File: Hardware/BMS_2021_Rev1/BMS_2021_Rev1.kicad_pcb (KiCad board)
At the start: 2 copper layers, 210.8 x 76.2 mm, 117 parts, among them Q1 2N7002PW, Q2 IRFS7530TRL7PP, Q3 IRFS7530TRL7PP, Q4 2N7002, Q5 2N7002PW, SW1 Relay_SPST, U1 TM4C129E_Launchpad, U2 ACS759ECB-200B-PFF-T, U3 TL3474ACPWR, U4 TL3474ACPWR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

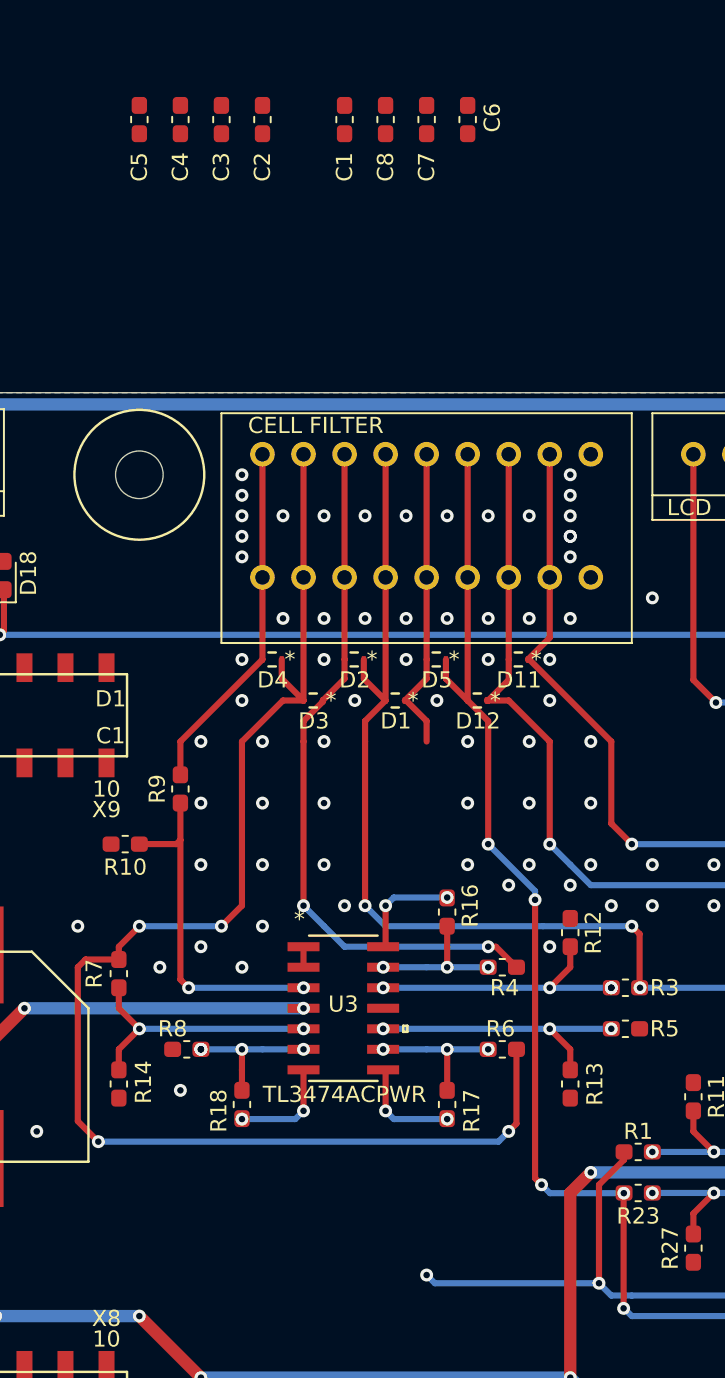
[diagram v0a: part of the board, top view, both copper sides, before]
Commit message: had forgot to add in cellFIlter Caps, added it (and kept the circuit well-grounded)
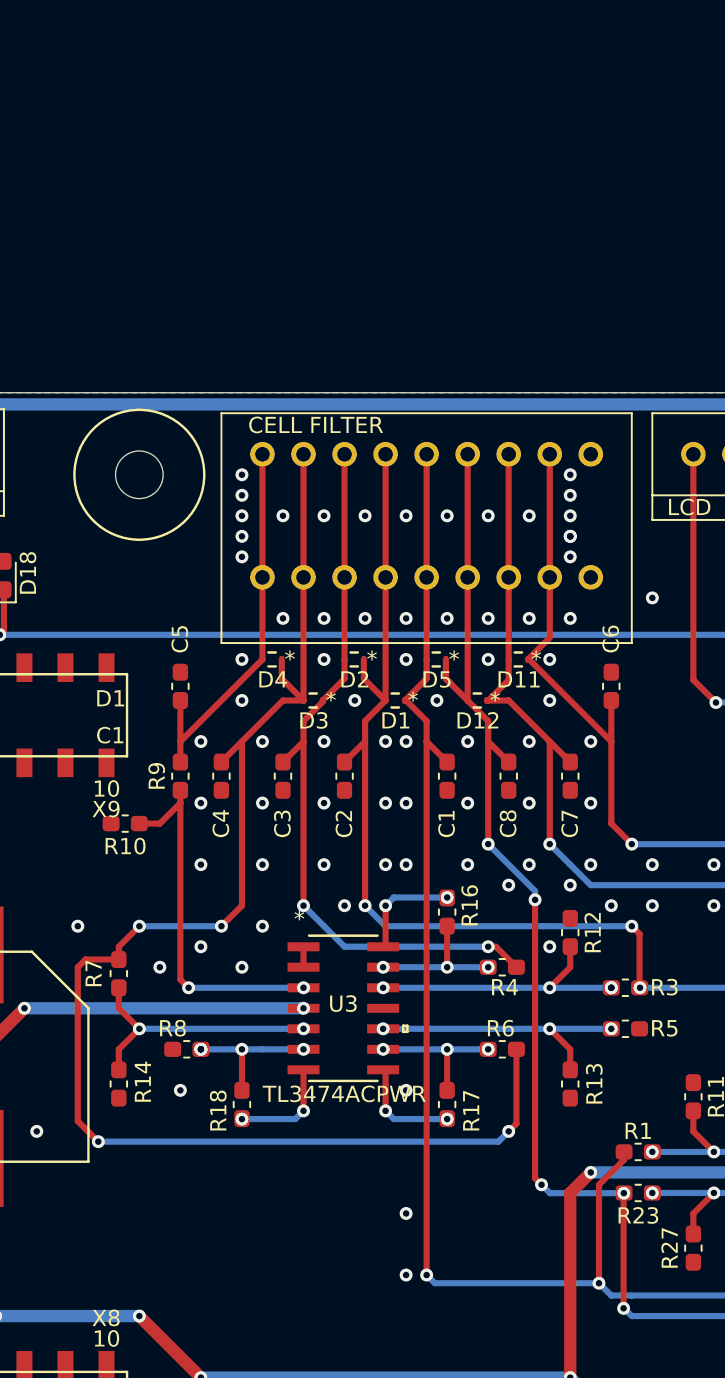
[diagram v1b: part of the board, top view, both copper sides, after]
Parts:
- moved C7 41.6 mm to (114.3, 49.1)
- moved C8 41.3 mm to (110.5, 49.1)
- moved C1 41.1 mm to (106.7, 49.1)
- moved C2 41.0 mm to (100.3, 49.1)
- moved C3 40.8 mm to (96.5, 49.1)
- moved C4 40.7 mm to (92.7, 49.1)
- moved C6 36.2 mm to (116.8, 43.6), turned to 270 degrees
- moved C5 35.2 mm to (90.2, 43.6), turned to 270 degrees
- moved R10 1.27 mm to (86.8, 52.1)
- moved R9 0.79 mm to (90.2, 49.1)
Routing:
- net cell_5_extension: track 52.7 -> 87.5 mm
- net /cell_8: track 88.7 -> 91.2 mm
- net /cell_6: track 97.9 -> 100.0 mm
- net /cell_4: track 67.7 -> 69.5 mm
- net /cell_3: track 43.8 -> 45.5 mm
- net /cell_2: track 87.8 -> 89.6 mm
- net /cell_7: track 98.9 -> 100.7 mm
- net /cell_1: track 21.9 -> 23.7 mm
- net Net-(R10-Pad1): track 21.4 -> 22.6 mm
- net GND: vias 131 -> 140

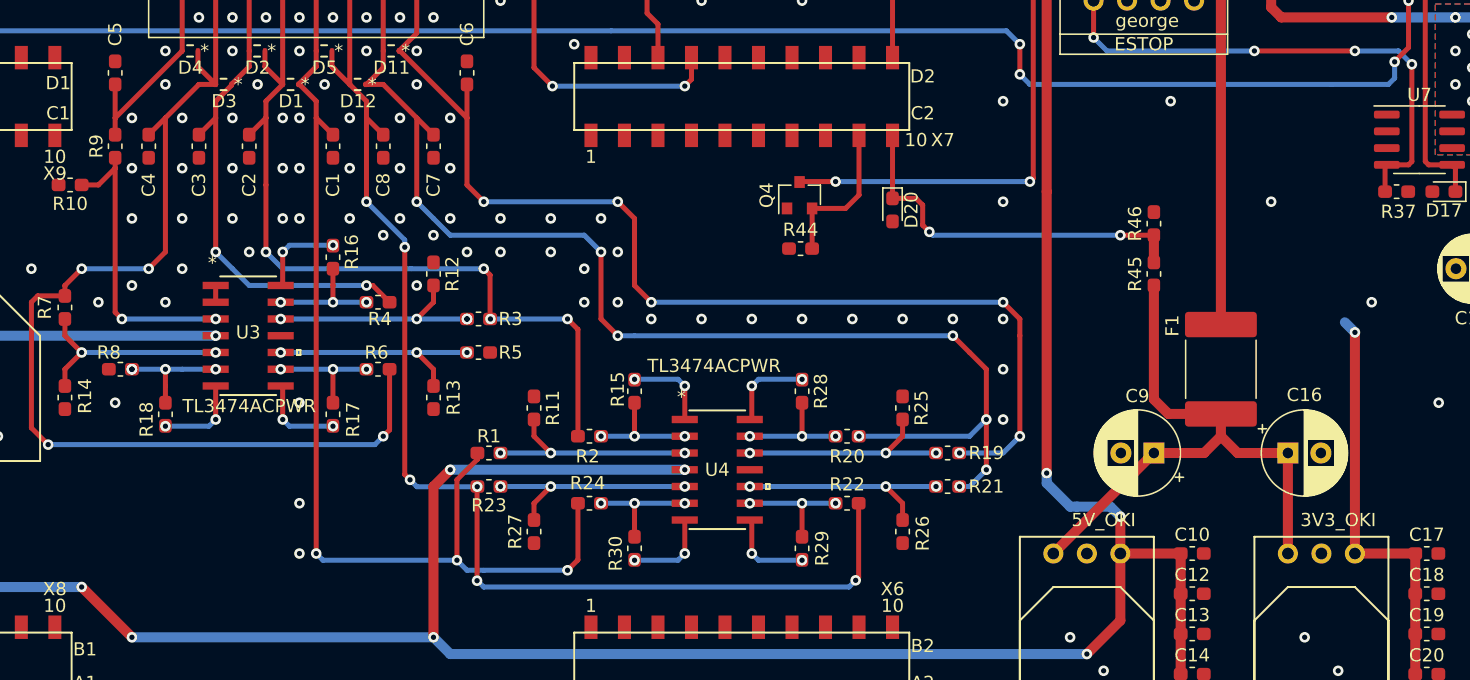
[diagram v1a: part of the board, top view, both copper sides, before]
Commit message: more gnd planing done btwn cell lines
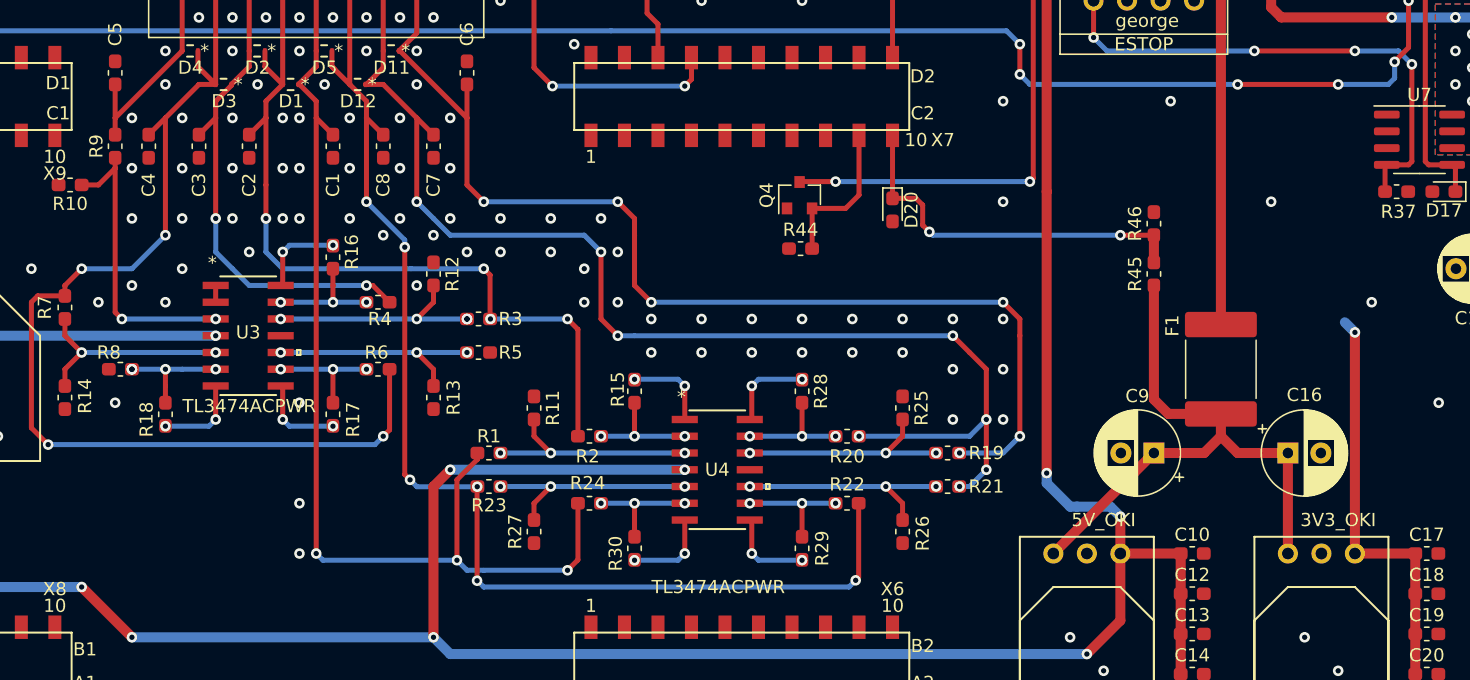
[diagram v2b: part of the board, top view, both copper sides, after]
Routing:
- net /cell_2: track 89.6 -> 88.9 mm
- net /V_out_sense: vias 6 -> 8
- net GND: vias 140 -> 148
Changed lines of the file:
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@@
     (thickness 1.6)
     (drawings 97)
-    (tracks 1187)
+    (tracks 1199)
     (zones 0)
     (modules 117)
@@
       (effects (font (size 1 1) (thickness 0.15)))
     )
-    (fp_text value TL3474ACPWR (at -0.2413 -7.874) (layer F.SilkS)
+    (fp_text value TL3474ACPWR (at 0.0762 8.89) (layer F.SilkS)
       (effects (font (size 1 1) (thickness 0.15)))
     )
@@
   (via (at 104.14 50.8) (size 0.8) (drill 0.4) (layers F.Cu B.Cu) (net 3))
   (via (at 102.87 54.61) (size 0.8) (drill 0.4) (layers F.Cu B.Cu) (net 3))
+  (via (at 130.81 64.77) (size 0.8) (drill 0.4) (layers F.Cu B.Cu) (net 3))
+  (via (at 134.62 64.77) (size 0.8) (drill 0.4) (layers F.Cu B.Cu) (net 3))
+  (via (at 138.43 64.77) (size 0.8) (drill 0.4) (layers F.Cu B.Cu) (net 3))
+  (via (at 142.24 64.77) (size 0.8) (drill 0.4) (layers F.Cu B.Cu) (net 3))
+  (via (at 146.05 64.77) (size 0.8) (drill 0.4) (layers F.Cu B.Cu) (net 3))
+  (via (at 149.86 64.77) (size 0.8) (drill 0.4) (layers F.Cu B.Cu) (net 3))
+  (via (at 153.67 66.04) (size 0.8) (drill 0.4) (layers F.Cu B.Cu) (net 3))
+  (via (at 153.67 69.85) (size 0.8) (drill 0.4) (layers F.Cu B.Cu) (net 3))
   (segment (start 102.87 29.21) (end 102.87 36.83) (width 0.381) (layer F.Cu) (net 4))
   (segment (start 102.87 36.83) (end 102.87 44.45) (width 0.381) (layer F.Cu) (net 4))
@@
   (segment (start 118.59 58.9) (end 118.11 58.42) (width 0.381) (layer F.Cu) (net 4))
   (segment (start 118.11 58.42) (end 112.6015 58.42) (width 0.381) (layer B.Cu) (net 4))
-  (via (at 101.6 57.15) (size 0.8) (drill 0.4) (layers F.Cu B.Cu) (net 4))
   (segment (start 112.6015 58.42) (end 102.87 58.42) (width 0.381) (layer B.Cu) (net 4))
   (segment (start 102.87 58.42) (end 101.6 57.15) (width 0.381) (layer B.Cu) (net 4))
-  (segment (start 101.6 57.15) (end 101.6 52.07) (width 0.381) (layer F.Cu) (net 4))
   (segment (start 101.6 52.07) (end 101.6 46.99) (width 0.381) (layer F.Cu) (net 4))
   (segment (start 100.33 48.26) (end 101.6 46.99) (width 0.381) (layer F.Cu) (net 4))
+  (via (at 101.6 54.61) (size 0.8) (drill 0.4) (layers F.Cu B.Cu) (net 4))
+  (segment (start 101.6 57.15) (end 101.6 54.61) (width 0.381) (layer B.Cu) (net 4))
+  (segment (start 101.6 54.61) (end 101.6 52.07) (width 0.381) (layer F.Cu) (net 4))
   (segment (start 100.33 29.21) (end 100.33 36.83) (width 0.381) (layer F.Cu) (net 5))
   (segment (start 100.33 36.83) (end 100.33 41.91) (width 0.381) (layer F.Cu) (net 5))
@@
   (segment (start 98.9838 44.5262) (end 97.79 45.72) (width 0.381) (layer F.Cu) (net 5))
   (segment (start 98.9838 44.45) (end 98.9838 44.5262) (width 0.381) (layer F.Cu) (net 5))
-  (segment (start 97.79 46.99) (end 97.79 57.15) (width 0.381) (layer F.Cu) (net 5))
-  (segment (start 97.79 57.15) (end 97.79 57.15) (width 0.381) (layer F.Cu) (net 5))
-  (via (at 97.79 57.15) (size 0.8) (drill 0.4) (layers F.Cu B.Cu) (net 5))
   (segment (start 99.06 58.42) (end 97.79 57.15) (width 0.381) (layer B.Cu) (net 5))
   (via (at 109.22 59.69) (size 0.8) (drill 0.4) (layers F.Cu B.Cu) (net 5))
@@
   (segment (start 109.22 59.69) (end 100.33 59.69) (width 0.381) (layer B.Cu) (net 5))
   (segment (start 96.52 48.26) (end 97.79 46.99) (width 0.381) (layer F.Cu) (net 5))
+  (via (at 97.79 54.61) (size 0.8) (drill 0.4) (layers F.Cu B.Cu) (net 5))
+  (segment (start 97.79 57.15) (end 97.79 54.61) (width 0.381) (layer B.Cu) (net 5))
+  (segment (start 97.79 54.61) (end 97.79 46.99) (width 0.381) (layer F.Cu) (net 5))
   (segment (start 97.79 29.21) (end 97.79 36.83) (width 0.381) (layer F.Cu) (net 6))
   (segment (start 97.79 36.83) (end 97.79 44.45) (width 0.381) (layer F.Cu) (net 6))
@@
   (segment (start 97.79 44.45) (end 96.52 44.45) (width 0.381) (layer F.Cu) (net 6))
   (segment (start 96.52 44.45) (end 93.98 46.99) (width 0.381) (layer F.Cu) (net 6))
-  (segment (start 93.98 46.99) (end 93.98 57.15) (width 0.381) (layer F.Cu) (net 6))
-  (via (at 92.71 58.42) (size 0.8) (drill 0.4) (layers F.Cu B.Cu) (net 6))
-  (segment (start 93.98 57.15) (end 92.71 58.42) (width 0.381) (layer F.Cu) (net 6))
-  (segment (start 92.71 58.42) (end 87.63 58.42) (width 0.381) (layer B.Cu) (net 6))
-  (via (at 87.63 58.42) (size 0.8) (drill 0.4) (layers F.Cu B.Cu) (net 6))
-  (segment (start 86.36 60.48) (end 86.36 59.69) (width 0.381) (layer F.Cu) (net 6))
-  (segment (start 86.36 59.69) (end 87.63 58.42) (width 0.381) (layer F.Cu) (net 6))
   (via (at 110.49 71.12) (size 0.8) (drill 0.4) (layers F.Cu B.Cu) (net 6))
   (segment (start 110.97 70.64) (end 110.97 66.04) (width 0.381) (layer F.Cu) (net 6))
@@
   (segment (start 85.09 71.755) (end 109.855 71.755) (width 0.381) (layer B.Cu) (net 6))
   (segment (start 92.71 48.26) (end 93.98 46.99) (width 0.381) (layer F.Cu) (net 6))
+  (via (at 93.98 55.88) (size 0.8) (drill 0.4) (layers F.Cu B.Cu) (net 6))
+  (segment (start 93.98 46.99) (end 93.98 55.88) (width 0.381) (layer F.Cu) (net 6))
+  (segment (start 93.98 55.88) (end 91.44 58.42) (width 0.381) (layer B.Cu) (net 6))
+  (segment (start 86.36 59.69) (end 87.63 58.42) (width 0.381) (layer F.Cu) (net 6))
+  (segment (start 86.36 60.48) (end 86.36 59.69) (width 0.381) (layer F.Cu) (net 6))
+  (via (at 87.63 58.42) (size 0.8) (drill 0.4) (layers F.Cu B.Cu) (net 6))
+  (segment (start 87.63 58.42) (end 91.44 58.42) (width 0.381) (layer B.Cu) (net 6))
   (segment (start 95.25 29.21) (end 95.25 36.83) (width 0.381) (layer F.Cu) (net 7))
   (segment (start 95.25 36.83) (end 95.25 41.91) (width 0.381) (layer F.Cu) (net 7))
@@
   (segment (start 79.248 37.592) (end 79.248 40.132) (width 0.381) (layer F.Cu) (net 28))
   (segment (start 158.75 41.402) (end 158.75 43.688) (width 0.381) (layer F.Cu) (net 28))
-  (segment (start 159.512 44.45) (end 182.372 44.45) (width 0.381) (layer B.Cu) (net 28))
   (segment (start 157.734 40.386) (end 158.75 41.402) (width 0.381) (layer B.Cu) (net 28))
   (segment (start 158.75 43.688) (end 159.512 44.45) (width 0.381) (layer B.Cu) (net 28))
@@
   (segment (start 187.161282 43.978718) (end 186.69 44.45) (width 0.381) (layer B.Cu) (net 28))
   (segment (start 187.161282 42.737218) (end 187.161282 43.978718) (width 0.381) (layer B.Cu) (net 28))
-  (segment (start 182.372 44.45) (end 186.69 44.45) (width 0.381) (layer B.Cu) (net 28))
+  (via (at 175.26 44.45) (size 0.8) (drill 0.4) (layers F.Cu B.Cu) (net 28))
+  (segment (start 159.512 44.45) (end 175.26 44.45) (width 0.381) (layer B.Cu) (net 28))
+  (via (at 182.88 44.45) (size 0.8) (drill 0.4) (layers F.Cu B.Cu) (net 28))
+  (segment (start 175.26 44.45) (end 182.88 44.45) (width 0.381) (layer F.Cu) (net 28))
+  (segment (start 182.88 44.45) (end 186.69 44.45) (width 0.381) (layer B.Cu) (net 28))
   (segment (start 149.098 48.1584) (end 149.098 53.086) (width 0.381) (layer F.Cu) (net 29))
   (segment (start 168.91 57.94) (end 168.91 55.88) (width 0.762) (layer F.Cu) (net 29))

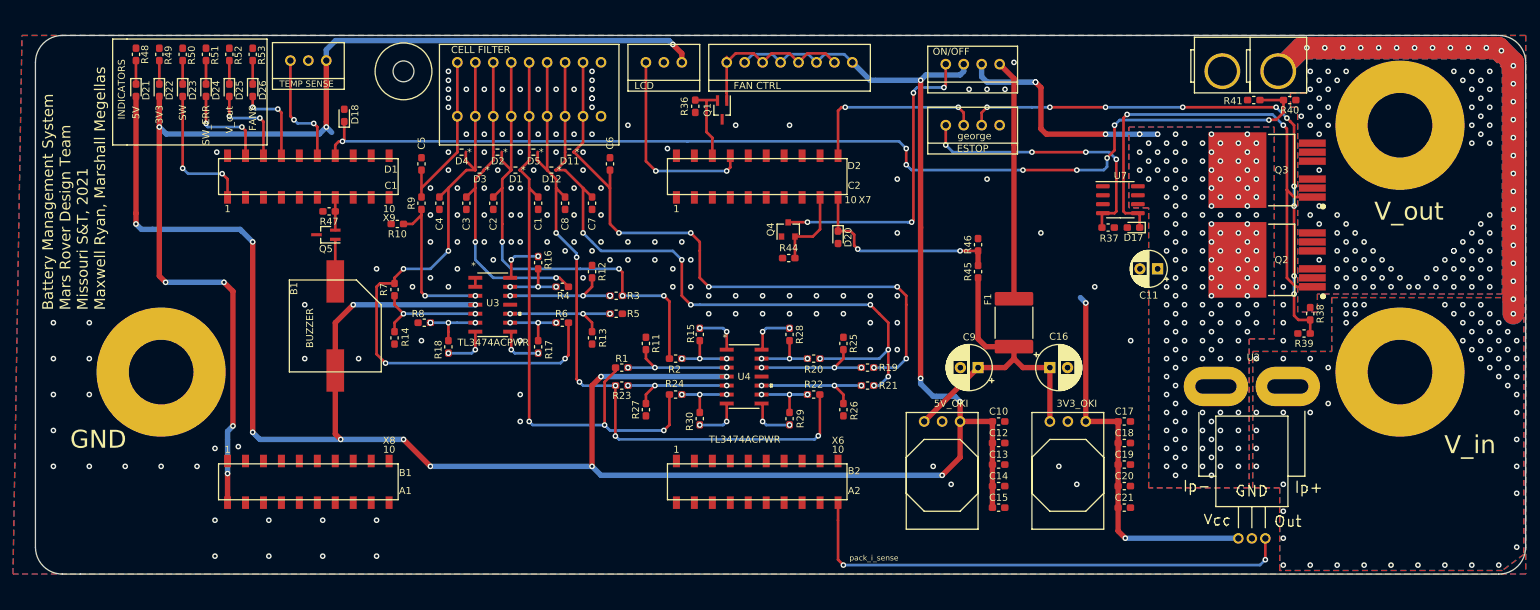
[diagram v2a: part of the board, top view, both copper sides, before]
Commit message: reinforce gnding around charging port
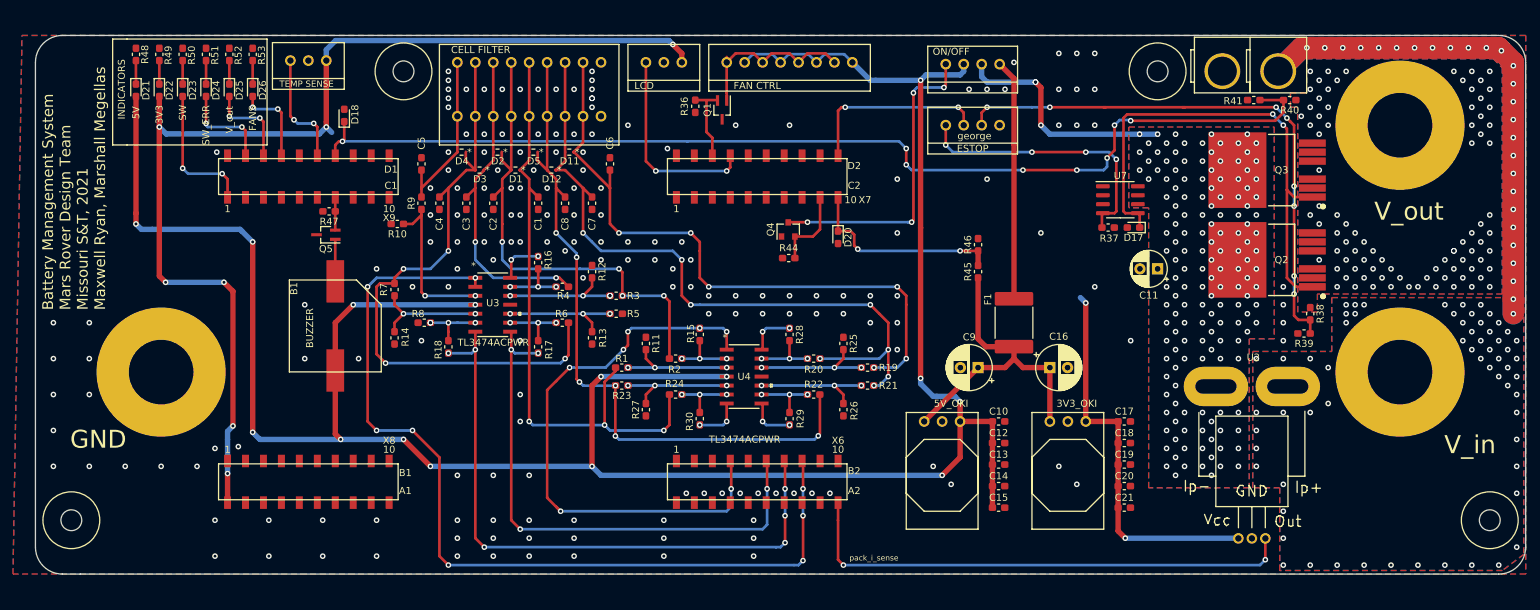
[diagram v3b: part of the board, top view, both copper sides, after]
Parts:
- added REF**: 4_40_Hole, MRDT_Drill_Holes:4_40_Hole, F.Cu at (194.3, 30.5)
- added REF**: 4_40_Hole, MRDT_Drill_Holes:4_40_Hole, F.Cu at (241.3, 94.0)
- added REF**: 4_40_Hole, MRDT_Drill_Holes:4_40_Hole, F.Cu at (40.6, 94.0)
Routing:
- net /cell_1_sense: track 1.36 -> 128.8 mm, vias 0 -> 8
- net /cell_2_sense: track 6.56 -> 89.4 mm, vias 2 -> 6
- net /cell_5_sense: track 6.65 -> 82.7 mm, vias 2 -> 7
- net /cell_3_sense: track 6.98 -> 77.2 mm, vias 2 -> 4
- net Net-(Conn5-Pad3): track 78.7 -> 79.2 mm, vias 10 -> 8
- net GND: vias 148 -> 185
